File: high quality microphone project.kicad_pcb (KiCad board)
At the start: 2 copper layers, 64.1 x 95 mm, 22 parts, among them U1 NMA0515SC

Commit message: pcb revision 1.1
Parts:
- added MH: MountingHole_3mm, MountingHole:MountingHole_3mm, F.Cu at (111.1, 54.2)
- added MH: MountingHole_3mm, MountingHole:MountingHole_3mm, F.Cu at (166.0, 54.1)
- added MH: MountingHole_3mm, MountingHole:MountingHole_3mm, F.Cu at (111.0, 140.0)
- added MH: MountingHole_3mm, MountingHole:MountingHole_3mm, F.Cu at (165.8, 140.1)
- moved G*** 62.1 mm to (119.8, 92.8), turned to 270 degrees
- moved DC 5V 6.60 mm to (156.9, 54.4)
- moved MIC 6.13 mm to (118.4, 54.1)
- moved GAIN 6.06 mm to (147.1, 54.3)
- moved AudioOut 5.41 mm to (137.8, 54.3)
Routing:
- net Net-(AudioOut1-Pad1): track 326.8 -> 312.7 mm
- net Net-(C1-Pad2): track 32.9 -> 28.0 mm
- net Net-(C6-Pad1): track 144.1 -> 146.6 mm
- net Net-(AudioOut1-Pad2): track 22.2 -> 24.2 mm
- net Net-(C2-Pad2): track 24.6 -> 26.3 mm
- net Net-(GAIN1-Pad2): track 59.8 -> 60.7 mm
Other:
- board text added: "Rev. 1.1"
- board text removed: "Rev. 1.0"

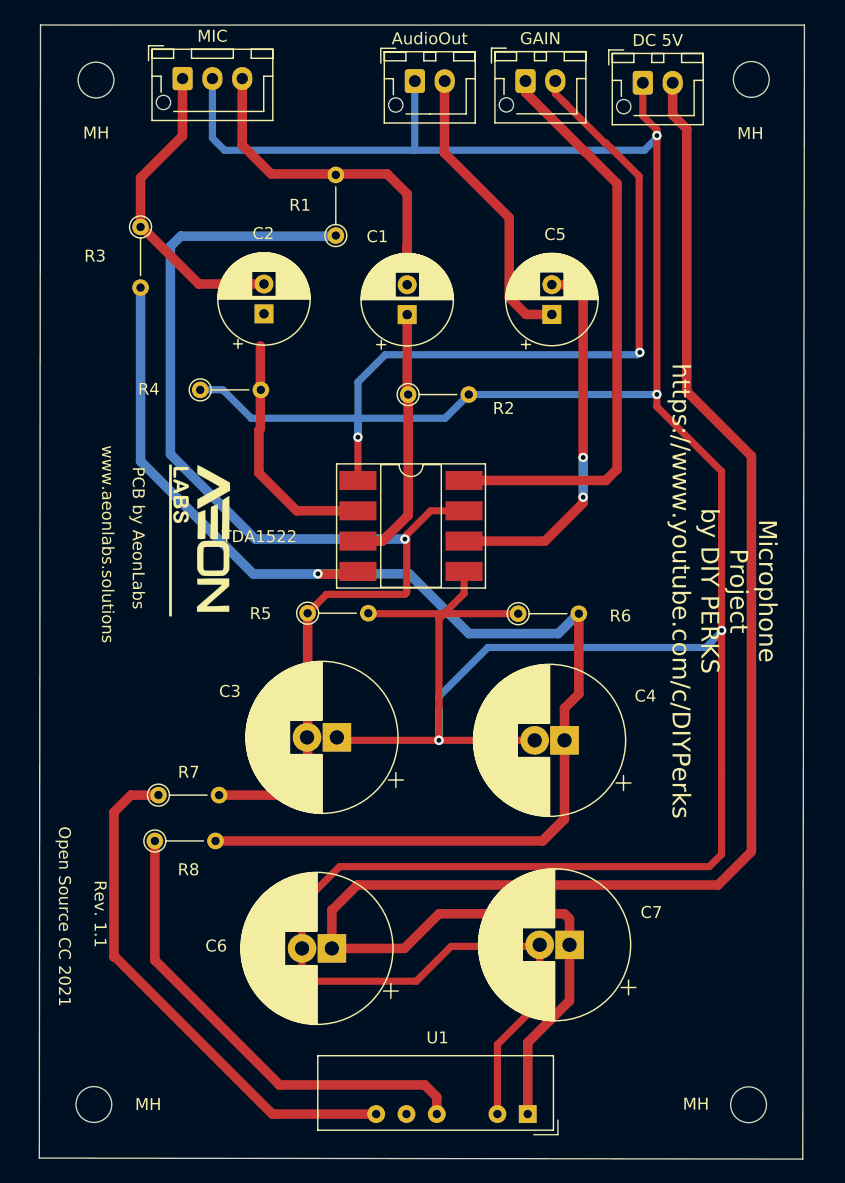
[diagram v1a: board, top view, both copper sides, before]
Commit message: Add files via upload
corrected a DRC error in a track.
Added Pinout text to the JST plugs
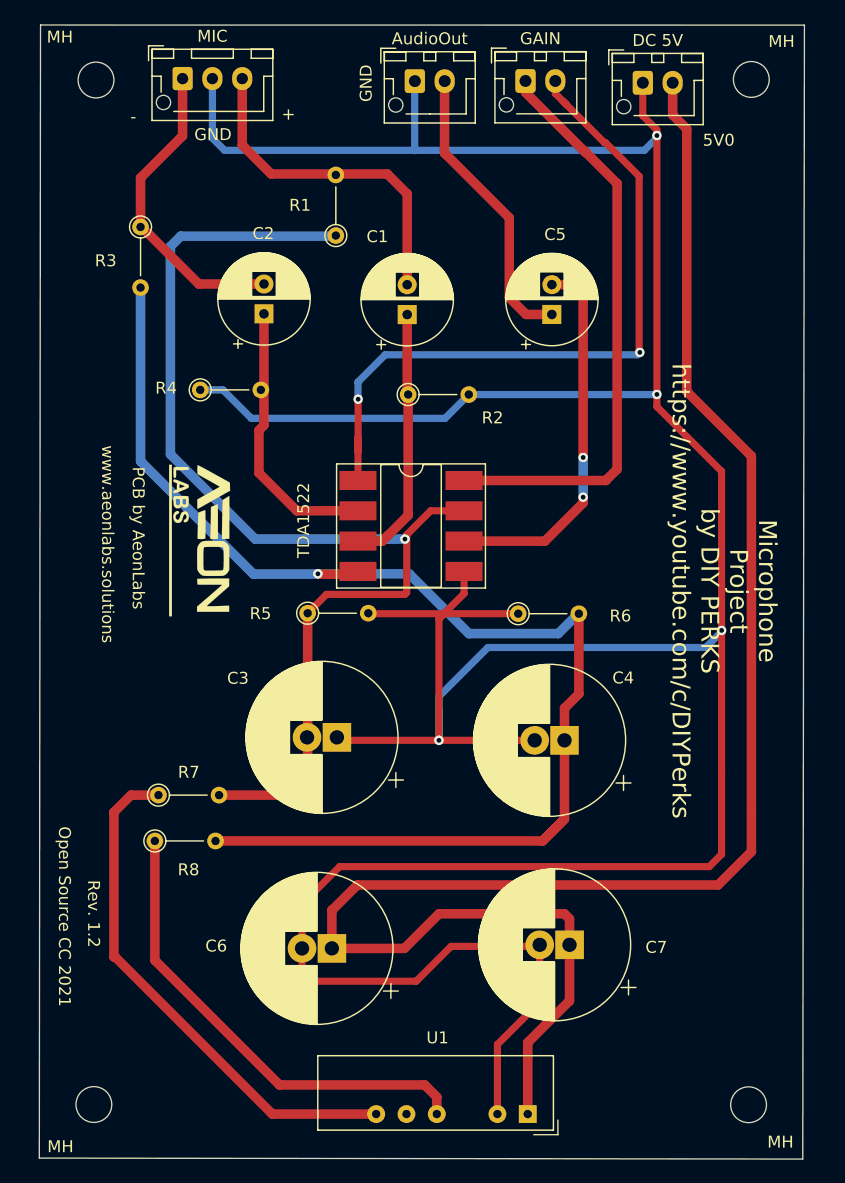
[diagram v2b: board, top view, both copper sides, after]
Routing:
- net Net-(C2-Pad1): track 20.3 -> 23.1 mm
- net Net-(C1-Pad2): track 28.0 -> 28.7 mm
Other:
- board text added: "+"
- board text added: "-"
- board text added: "5V0"
- board text added: "GND"
- board text added: "Rev. 1.2"
- board text removed: "Rev. 1.1"
